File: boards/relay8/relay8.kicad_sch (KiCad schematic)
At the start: 56 parts, among them J1 USB-C, J11 CH1, J12 CH2, J13 CH3, J14 CH4, J15 CH5, J16 CH6, J17 CH7, J18 CH8, J2 UART, J3 5V DC 2A, K1 SRD-05VDC-SL-C, K2 SRD-05VDC-SL-C, K3 SRD-05VDC-SL-C, K4 SRD-05VDC-SL-C, K5 SRD-05VDC-SL-C, K6 SRD-05VDC-SL-C, K7 SRD-05VDC-SL-C, K8 SRD-05VDC-SL-C, SW1 RESET, SW2 BOOT, U1 ESP32-C3-WROOM-02-N4, U2 AP2112K-3.3, U3 ULN2803A

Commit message: relay8 v2: one mains cable powers everything
The board now takes mains on a single L/N input (J20) instead of a
5 V DC jack plus per-channel feeds:

- J20 -> F1 (T8A, 5x20) -> L bus -> COM of all 8 relays
- N bus from J20 to the middle pin of every output terminal, so each
  appliance connects live and neutral at one terminal: NC . N . NO
- RV1 14D431K across L/N after the fuse
- F2 (T1A, TR5) -> HLK-10M05 (100-240 VAC -> 5 V 2 A) for the relay
  coils and, through the existing diode-OR, the 3.3 V logic

Both buses run on B.Cu (6.5 mm); NO/NC cross them on F.Cu (3.5 mm),
so the layers are separated by the laminate. The F1 exit feeds the L
bus directly and F2 is tapped with a thin trace: routing the bus
through F2's pad left 2.33 mm to F2's other pin (TR5 pitch is 5.1 mm).
Ratings: 5 A per channel, 8 A total. MetzConnect Type171 7.5 mm
terminals; their wire-entry side is not verifiable from KiCad's files
and is listed as a pre-order check.

ERC 0, netlist check 211/211 pins, DRC errors 0, unconnected 0,
schematic parity; 40 silkscreen-clipped-by-slot/edge warnings.
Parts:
- removed J3: 5V DC 2A, Connector_BarrelJack:BarrelJack_Horizontal, symbol Connector:Barrel_Jack
- added F1: T8A 250V, Fuse:Fuseholder_Clip-5x20mm_Keystone_3517_Inline_P23.11x6.76mm_D1.70mm_Horizontal, symbol Device:Fuse
- added F2: T1A 250V, Fuse:Fuseholder_TR5_Littelfuse_No560_No460, symbol Device:Fuse
- added J20: MAINS IN, TerminalBlock_MetzConnect:TerminalBlock_MetzConnect_Type171_RT13702HBWC_1x02_P7.50mm_Horizontal, symbol Connector:Screw_Terminal_01x02
- added PS1: HLK-10M05, Converter_ACDC:Converter_ACDC_Hi-Link_HLK-10Mxx, symbol Converter_ACDC:HLK-10M05
- added RV1: 14D431K, Varistor:RV_Disc_D15.5mm_W4.4mm_P7.5mm, symbol Device:Varistor
- J11, J12, J13, J14, J15, J16, J17, J18: footprint TerminalBlock_Phoenix:TerminalBlock_Phoenix_MKDS-1,5-3-5.08_1x03_P5.08mm_Horizontal -> TerminalBlock_MetzConnect:TerminalBlock_MetzConnect_Type171_RT13703HBWC_1x03_P7.50mm_Horizontal
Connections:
- net GND: now also PS1.3 (-Vout)
- net DC_IN renamed 5V_PS
- net 5V_PS: now also PS1.4 (+Vout)
- net RL1_COM renamed L_BUS
- net L_BUS: now also K2.1, K3.1, K4.1, K5.1, K6.1, K7.1, K8.1, F1.2, F2.1, RV1.1; no longer J11.2 (Pin_2)
- net RL2_COM renamed N_BUS
- net N_BUS: now also J11.2 (Pin_2), J13.2 (Pin_2), J14.2 (Pin_2), J15.2 (Pin_2), J16.2 (Pin_2), J17.2 (Pin_2), J18.2 (Pin_2), J20.2 (Pin_2), PS1.2 (AC/N), RV1.2; no longer K2.1
- removed net RL3_COM: J13.2 (Pin_2), K3.1
- removed net RL4_COM: J14.2 (Pin_2), K4.1
- removed net RL5_COM: J15.2 (Pin_2), K5.1
- removed net RL6_COM: J16.2 (Pin_2), K6.1
- removed net RL7_COM: J17.2 (Pin_2), K7.1
- removed net RL8_COM: J18.2 (Pin_2), K8.1
- new net L_IN: F1.1, J20.1 (Pin_1)
- new net L_PS: F2.2, PS1.1 (AC/L)

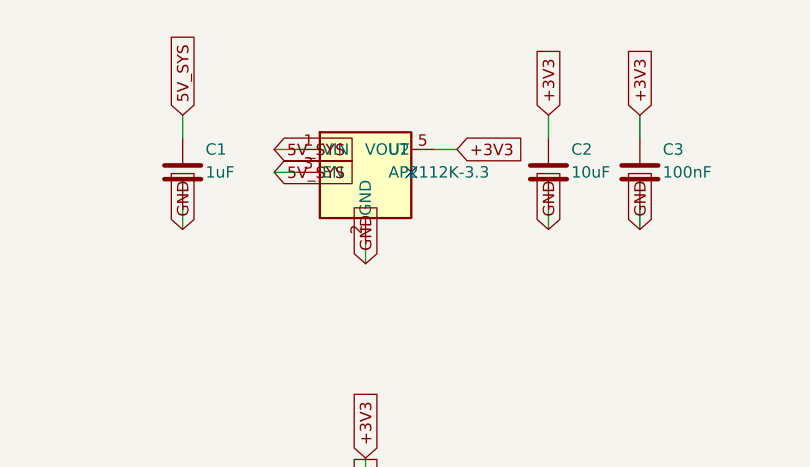
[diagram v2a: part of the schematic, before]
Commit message: esp32c3, relay8: LP38693 instead of AP2112K (hot-plug overshoot exceeded 6.5 V)
With only 1 uF on VBUS, cable ringing on hot-plug reaches 8.6 V (esp32c3) and
7.7 V (relay8, through SS34) at the LDO input; AP2112K's absolute maximum is
6.5 V. The USBLC6 VBUS zener lowers it by ~0.6 V, not enough. LP38693 is rated
12 V. New boards/esp32c3/sim/power_sim.py covers both boards and includes the
module's own ~12.3 uF (WROOM-02 datasheet fig. 8-1): total hot-plug charge is
~79 uC, over USB 2.0's 50 uC; documented as a compliance limitation.
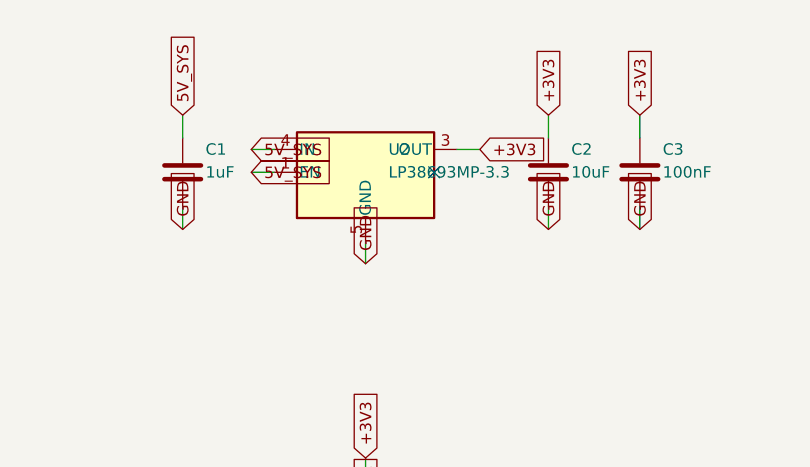
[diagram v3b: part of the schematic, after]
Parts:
- removed U2: AP2112K-3.3, Package_TO_SOT_SMD:SOT-23-5, symbol Regulator_Linear:AP2112K-3.3
- added U2: LP38693MP-3.3, Package_TO_SOT_SMD:SOT-223-5, symbol Regulator_Linear:LP38693MP-3.3
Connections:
- net +3V3: now also U2.3 (OUT)
- net 5V_SYS: now also U2.1 (EN), U2.4 (IN)
- net GND: now also U2.5 (GND)

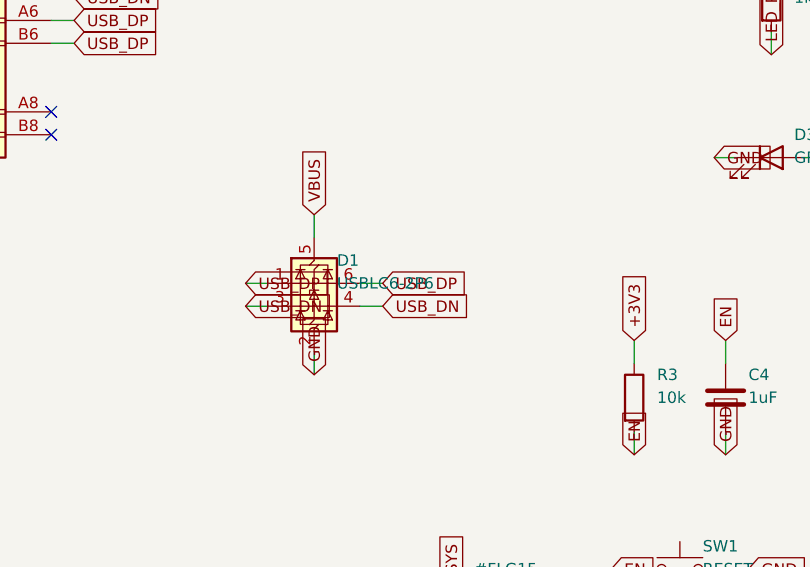
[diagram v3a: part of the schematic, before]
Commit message: fab: Gerber/drill zip + JLCPCB BOM/CPL with self-checks; USBLC6-2SC6 to match SOT-23-6
lib/fab.py runs as the last build step on all three boards. It refuses to
write the zip when a required Gerber layer is missing or empty, when the
drill-hit count differs from vias + plated/NPTH pad holes (route-format
slots counted once), or when BOM / CPL / board refdes sets disagree.

It also compares each symbol's library default footprint with the one
actually assigned. That caught all three boards using the USBLC6-2P6
symbol (SOT-666) on a SOT-23-6 footprint: electrically identical pinout,
so ERC/DRC/netlist checks passed, but a BOM ordered by value would buy a
part that does not fit. Switched to USBLC6-2SC6.

LCSC part numbers come from a hand-checked boards/<b>/lcsc.json; the
script never guesses them and lists missing rows in fab/missing-lcsc.txt.
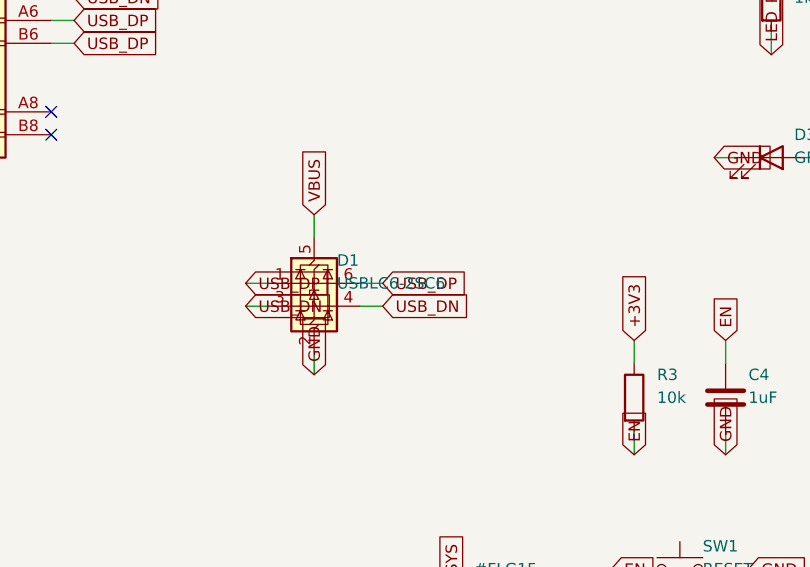
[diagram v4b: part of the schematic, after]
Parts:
- removed D1: USBLC6-2P6, Package_TO_SOT_SMD:SOT-23-6, symbol Power_Protection:USBLC6-2P6
- added D1: USBLC6-2SC6, Package_TO_SOT_SMD:SOT-23-6, symbol Power_Protection:USBLC6-2SC6
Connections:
- net GND: now also D1.2 (GND)
- net USB_DN: now also D1.3 (I/O2), D1.4 (I/O2)
- net USB_DP: now also D1.1 (I/O1), D1.6 (I/O1)
- net VBUS: now also D1.5 (VBUS)

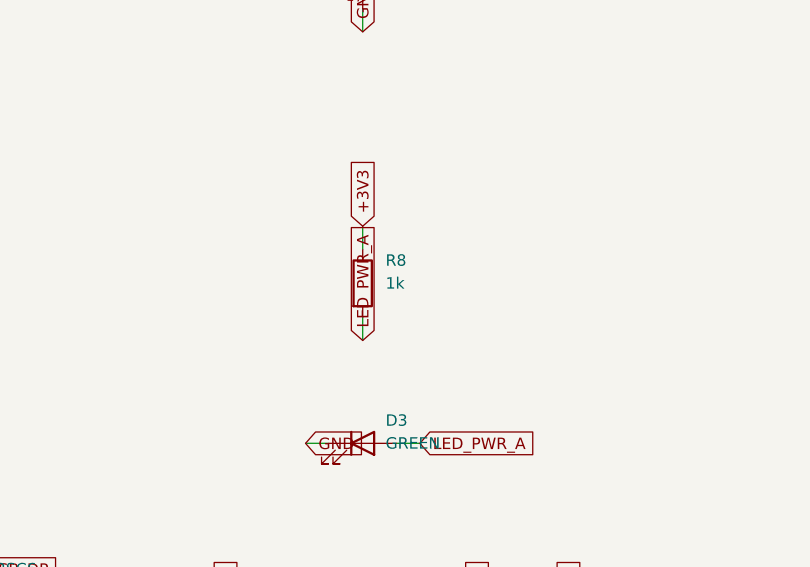
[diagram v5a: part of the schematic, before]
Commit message: review: datasheet design review on the netlist; fixes a reversed TVS and dim LEDs
lib/review.py checks the design intent that ERC and the netlist check take
on trust: diode/TVS polarity against inferred rail voltages, LED current
from the JLC Vf range, per-datasheet decoupling and supply ranges, USB-C
CC pull-downs and D+/D- on both sides, ESP32-C3 EN RC, strapping pins and
GPIO18/19, relay flyback path and pickup voltage, capacitor rating and
polarity. It runs after the netlist check and stops the build on ERROR.
lib/review_test.py breaks the real netlists 15 ways; every rule fires and
the unmodified boards report no ERROR.

Real defects it found:
- usbc-ldo: SMAJ5.0A had anode on +5V and cathode on GND (KiCad names
  the cathode pin "A1"), shorting the rail on plug-in. Swapped.
- esp32c3: blue user LED on a 3.3 V GPIO (Vf 2.5-3.6 V) -> yellow, 470R.
- esp32c3, relay8: green power LED at ~0.45 mA through 1k -> 220R.
- usbc-ldo: SS32 symbol for an SS34 part -> Diode:SS34.

Also: lcsc-check.json keeps JLC attributes (Vf, voltage rating) for the
review; lcsc.py groups parts from net.txt instead of fab/groups.json; the
build retries freerouting (up to 3 runs) because it is not deterministic
and occasionally leaves two connections unrouted on the same DSN.
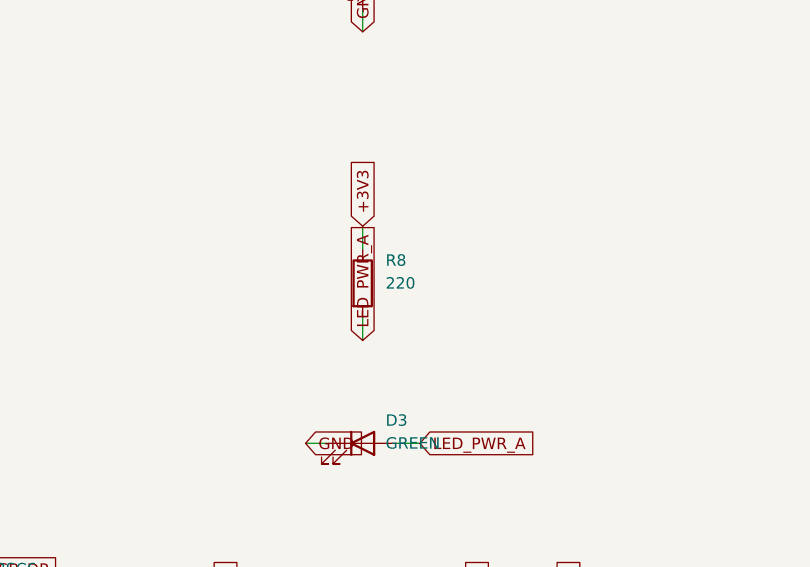
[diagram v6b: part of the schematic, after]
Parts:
- R8: value 1k -> 220

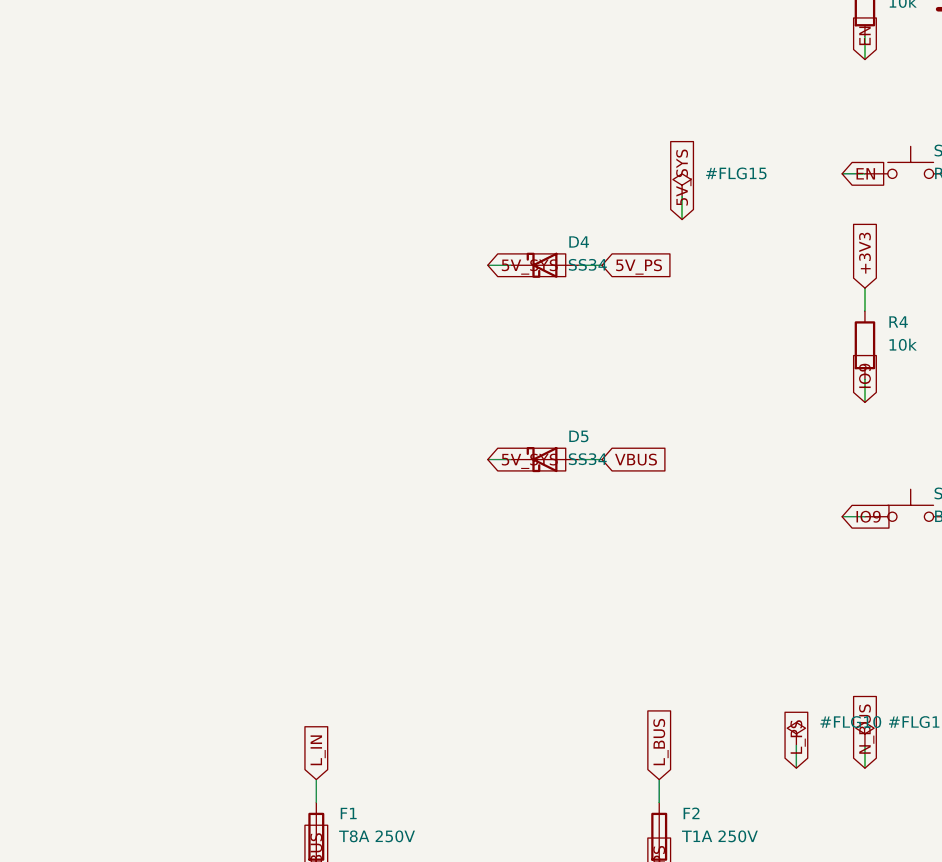
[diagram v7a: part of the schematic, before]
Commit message: relay8: VBUS soft-start (AO3401A) keeps USB hot-plug inrush within USB 2.0
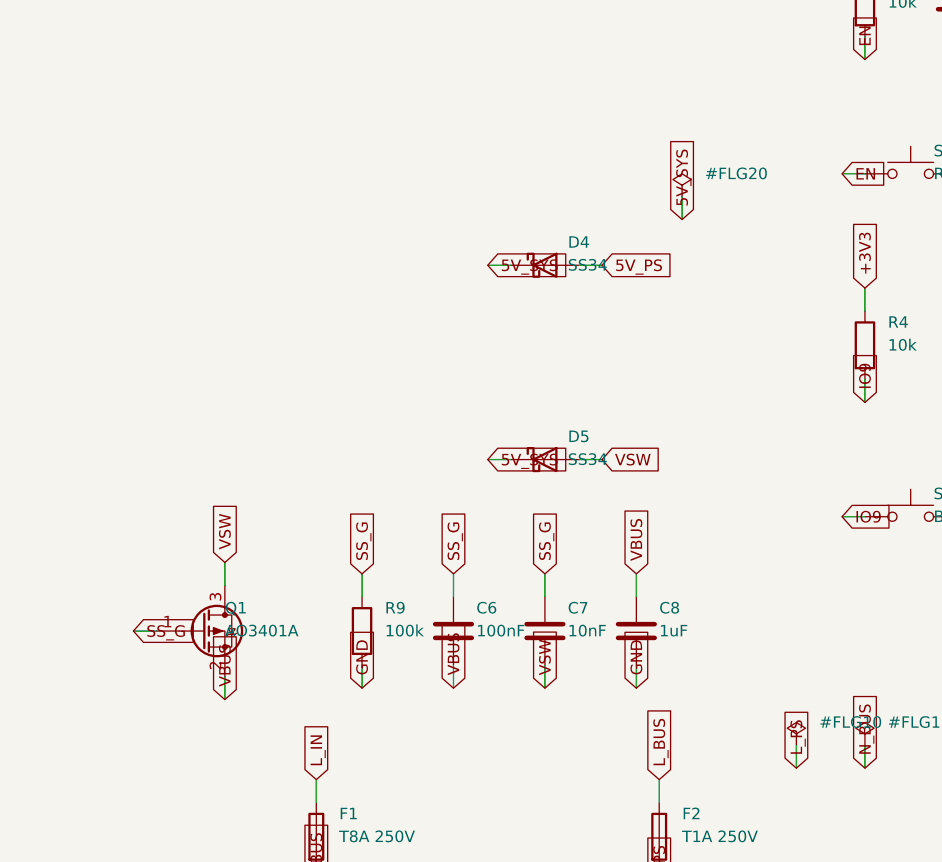
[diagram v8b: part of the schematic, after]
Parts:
- removed D11: RED, LED_SMD:LED_0805_2012Metric, symbol Device:LED
- removed J11: CH1, TerminalBlock_MetzConnect:TerminalBlock_MetzConnect_Type171_RT13703HBWC_1x03_P7.50mm_Horizontal, symbol Connector:Screw_Terminal_01x03
- removed K1: SRD-05VDC-SL-C, Relay_THT:Relay_SPDT_SANYOU_SRD_Series_Form_C, symbol Relay:SANYOU_SRD_Form_C
- removed R11: 1k, Resistor_SMD:R_0402_1005Metric, symbol Device:R
- added C6: 100nF, Capacitor_SMD:C_0402_1005Metric, symbol Device:C
- added C7: 10nF, Capacitor_SMD:C_0402_1005Metric, symbol Device:C
- added C8: 1uF, Capacitor_SMD:C_0402_1005Metric, symbol Device:C
- added D18: RED, LED_SMD:LED_0805_2012Metric, symbol Device:LED
- added J18: CH8, TerminalBlock_MetzConnect:TerminalBlock_MetzConnect_Type171_RT13703HBWC_1x03_P7.50mm_Horizontal, symbol Connector:Screw_Terminal_01x03
- added K8: SRD-05VDC-SL-C, Relay_THT:Relay_SPDT_SANYOU_SRD_Series_Form_C, symbol Relay:SANYOU_SRD_Form_C
- added Q1: AO3401A, Package_TO_SOT_SMD:SOT-23, symbol Transistor_FET:AO3401A
- added R18: 1k, Resistor_SMD:R_0402_1005Metric, symbol Device:R
- added R9: 100k, Resistor_SMD:R_0402_1005Metric, symbol Device:R
- J11: renamed from J12; value CH2 -> CH1
- J12: renamed from J13; value CH3 -> CH2
- J13: renamed from J14; value CH4 -> CH3
- J14: renamed from J15; value CH5 -> CH4
- J15: renamed from J16; value CH6 -> CH5
- J16: renamed from J17; value CH7 -> CH6
- J17: renamed from J18; value CH8 -> CH7
- renumbered D12 to D11, D13 to D12, D14 to D13, D15 to D14, D16 to D15, D17 to D16, D18 to D17, K2 to K1, K3 to K2, K4 to K3, K5 to K4, K6 to K5, K7 to K6, K8 to K7, R12 to R11, R13 to R12, R14 to R13, R15 to R14, R16 to R15, R17 to R16, R18 to R17
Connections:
- net 5V_PS: now also K8.5, R18.1
- net GND: now also C8.2, R9.2
- net LED1_A: now also D11.2 (A), R11.2
- net LED2_A: now also D12.2 (A), R12.2; no longer D11.2 (A), R11.2
- net LED3_A: now also D13.2 (A), R13.2; no longer D12.2 (A), R12.2
- net LED4_A: now also D14.2 (A), R14.2; no longer D13.2 (A), R13.2
- net LED5_A: now also D15.2 (A), R15.2; no longer D14.2 (A), R14.2
- net LED6_A: now also D16.2 (A), R16.2; no longer D15.2 (A), R15.2
- net LED7_A: now also D17.2 (A), R17.2; no longer D16.2 (A), R16.2
- net LED8_A: now also D18.2 (A), R18.2; no longer D17.2 (A), R17.2
- net L_BUS: now also K8.1
- net N_BUS: now also J18.2 (Pin_2)
- net RL1_NC: now also J11.3 (Pin_3), K1.4
- net RL1_NO: now also J11.1 (Pin_1), K1.3
- net RL2_NC: now also J12.3 (Pin_3), K2.4; no longer J11.3 (Pin_3), K1.4
- net RL2_NO: now also J12.1 (Pin_1), K2.3; no longer J11.1 (Pin_1), K1.3
- net RL3_NC: now also J13.3 (Pin_3), K3.4; no longer J12.3 (Pin_3), K2.4
- net RL3_NO: now also J13.1 (Pin_1), K3.3; no longer J12.1 (Pin_1), K2.3
- net RL4_NC: now also J14.3 (Pin_3), K4.4; no longer J13.3 (Pin_3), K3.4
- net RL4_NO: now also J14.1 (Pin_1), K4.3; no longer J13.1 (Pin_1), K3.3
- net RL5_NC: now also J15.3 (Pin_3), K5.4; no longer J14.3 (Pin_3), K4.4
- net RL5_NO: now also J15.1 (Pin_1), K5.3; no longer J14.1 (Pin_1), K4.3
- net RL6_NC: now also J16.3 (Pin_3), K6.4; no longer J15.3 (Pin_3), K5.4
- net RL6_NO: now also J16.1 (Pin_1), K6.3; no longer J15.1 (Pin_1), K5.3
- net RL7_NC: now also J17.3 (Pin_3), K7.4; no longer J16.3 (Pin_3), K6.4
- net RL7_NO: now also J17.1 (Pin_1), K7.3; no longer J16.1 (Pin_1), K6.3
- net RL8_NC: now also J18.3 (Pin_3), K8.4; no longer J17.3 (Pin_3), K7.4
- net RL8_NO: now also J18.1 (Pin_1), K8.3; no longer J17.1 (Pin_1), K7.3
- net RLY1: now also D11.1 (K), K1.2
- net RLY2: now also D12.1 (K), K2.2; no longer D11.1 (K), K1.2
- net RLY3: now also D13.1 (K), K3.2; no longer D12.1 (K), K2.2
- net RLY4: now also D14.1 (K), K4.2; no longer D13.1 (K), K3.2
- net RLY5: now also D15.1 (K), K5.2; no longer D14.1 (K), K4.2
- net RLY6: now also D16.1 (K), K6.2; no longer D15.1 (K), K5.2
- net RLY7: now also D17.1 (K), K7.2; no longer D16.1 (K), K6.2
- net RLY8: now also D18.1 (K), K8.2; no longer D17.1 (K), K7.2
- net VBUS: now also C6.2, C8.1, Q1.2 (S); no longer D5.2 (A)
- new net SS_G: C6.1, C7.1, Q1.1 (G), R9.1
- new net VSW: C7.2, D5.2 (A), Q1.3 (D)
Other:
- moved on the sheet: D11, D12, D13, D14, D15, D16, D17, J11, J12, J13, J14, J15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
